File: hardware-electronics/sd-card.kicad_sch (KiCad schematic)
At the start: 40 parts, among them J5 Micro_SD_Card_Det_Hirose_DM3AT, U6 24AA04T-I_OT, U9 USB2244-AEZG-06, Y3 ECS-240-10-47-CKM-TR

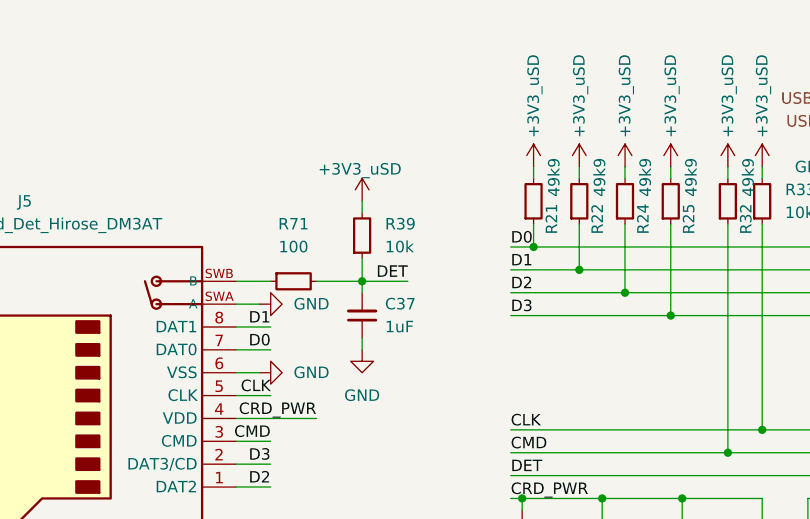
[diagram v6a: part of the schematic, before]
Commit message: [#16] uSD decreased cap reload time to aprox 10ms on DET pins
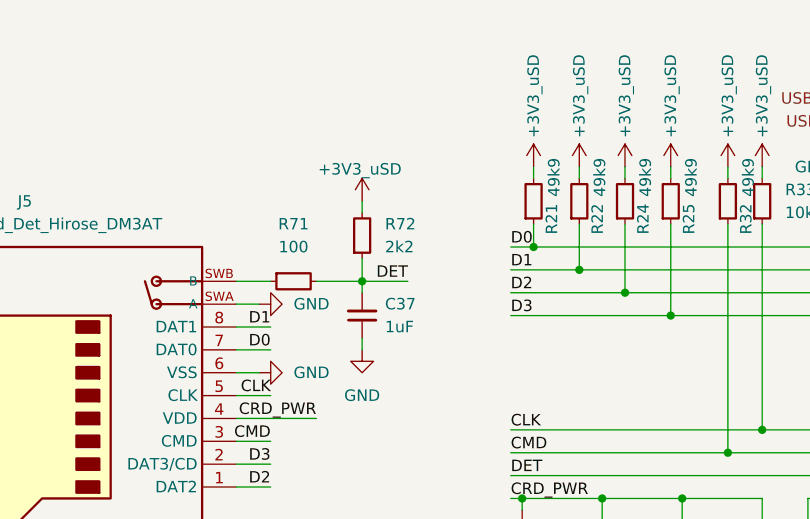
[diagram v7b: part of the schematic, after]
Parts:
- removed R39: R_10k_0402, M2SmartHomeFootprints:R_0402, symbol M2SmartHomeSymbols:R_10k_0402
- added R72: R_2k2_0402, M2SmartHomeFootprints:R_0402, symbol M2SmartHomeSymbols:R_2k2_0402
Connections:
- net +3V3_uSD: now also R72.2
- net DET: now also R72.1
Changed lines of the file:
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@@
-	)
-	(symbol
-		(lib_id "M2SmartHomeSymbols:R_10k_0402")
-		(at 78.74 72.39 90)
-		(unit 1)
-		(exclude_from_sim no)
-		(in_bom yes)
-		(on_board yes)
-		(dnp no)
-		(fields_autoplaced yes)
-		(property "Reference" "R39"
-			(at 81.28 68.58 90)
-			(effects
-				(font
-					(size 1.27 1.27)
-					(thickness 0.15)
-				)
-				(justify right)
-			)
-		)
-		(property "Value" "R_10k_0402"
-			(at 91.44 52.07 0)
-			(effects
-				(font
-					(size 1.27 1.27)
-					(thickness 0.15)
-				)
-				(justify left bottom)
-				(hide yes)
-			)
-		)
-		(property "Footprint" "M2SmartHomeFootprints:R_0402"
-			(at 93.98 52.07 0)
-			(effects
-				(font
-					(size 1.27 1.27)
-					(thickness 0.15)
-				)
-				(justify left bottom)
-				(hide yes)
-			)
-		)
-		(property "Datasheet" "https://www.vishay.com/docs/20035/crcw0402.pdf"
-			(at 96.52 52.07 0)
-			(effects
-				(font
-					(size 1.27 1.27)
-					(thickness 0.15)
-				)
-				(justify left bottom)
-				(hide yes)
-			)
-		)
-		(property "Description" "SMD Thick Film Resistor, 10 kΩ, ±1%, 1/16 W, 0402 [1005 Metric], CRCW Series"
-			(at 78.74 72.39 0)
-			(effects
-				(font
-					(size 1.27 1.27)
-				)
-				(hide yes)
-			)
-		)
-		(property "MPN" "CRCW040210K0FKED"
-			(at 99.06 52.07 0)
-			(effects
-				(font
-					(size 1.27 1.27)
-					(thickness 0.15)
-				)
-				(justify left bottom)
-				(hide yes)
-			)
-		)
-		(property "Manufacturer" "Vishay"
-			(at 101.6 52.07 0)
-			(effects
-				(font
-					(size 1.27 1.27)
-					(thickness 0.15)
-				)
-				(justify left bottom)
-				(hide yes)
-			)
-		)
-		(property "License" "Apache-2.0"
-			(at 104.14 52.07 0)
-			(effects
-				(font
-					(size 1.27 1.27)
-					(thickness 0.15)
-				)
-				(justify left bottom)
-				(hide yes)
-			)
-		)
-		(property "Author" "Your Name"
-			(at 106.68 52.07 0)
-			(effects
-				(font
-					(size 1.27 1.27)
-					(thickness 0.15)
-				)
-				(justify left bottom)
-				(hide yes)
-			)
-		)
-		(property "Val" "10k"
-			(at 81.28 71.12 90)
-			(effects
-				(font
-					(size 1.27 1.27)
-					(thickness 0.15)
-				)
-				(justify right)
-			)
-		)
-		(property "Tolerance" "1%"
-			(at 88.9 52.07 0)
-			(effects
-				(font
-					(size 1.27 1.27)
-				)
-				(justify left bottom)
-				(hide yes)
-			)
-		)
-		(property "Power" "1/16 W"
-			(at 92.44 52.07 0)
-			(effects
-				(font
-					(size 1.27 1.27)
-				)
-				(justify left bottom)
-				(hide yes)
-			)
-		)
-		(pin "1"
-		)
-		(pin "2"
-		)
-		(instances
-			(project "M2SmartHome"
-				(path "/da663dec-9e91-4003-a791-431d460ad63c/2a53ffe2-5715-44b3-b464-b3185e5be86d"
-					(reference "R39")
-					(unit 1)
-				)
-			)
-		)
 	)
 	(symbol
@@
 					(unit 1)
 				)
+			)
+		)
+	)
+	(symbol
+		(lib_id "M2SmartHomeSymbols:R_2k2_0402")
+		(at 78.74 72.39 90)
+		(unit 1)
+		(exclude_from_sim no)
+		(in_bom yes)
+		(on_board yes)
+		(dnp no)
+		(fields_autoplaced yes)
+		(property "Reference" "R72"
+			(at 81.28 68.58 90)
+			(effects
+				(font
+					(size 1.27 1.27)
+					(thickness 0.15)
+				)
+				(justify right)
+			)
+		)
+		(property "Value" "R_2k2_0402"
+			(at 91.44 52.07 0)
+			(effects
+				(font
+					(size 1.27 1.27)
+					(thickness 0.15)
+				)
+				(justify left bottom)
+				(hide yes)
+			)
+		)
+		(property "Footprint" "M2SmartHomeFootprints:R_0402"
+			(at 93.98 52.07 0)
+			(effects
+				(font
+					(size 1.27 1.27)
+					(thickness 0.15)
+				)
+				(justify left bottom)
+				(hide yes)
+			)
+		)
+		(property "Datasheet" "https://www.vishay.com/docs/20035/crcw0402.pdf"
+			(at 96.52 52.07 0)
+			(effects
+				(font
+					(size 1.27 1.27)
+					(thickness 0.15)
+				)
+				(justify left bottom)
+				(hide yes)
+			)
+		)
+		(property "Description" "SMD Thick Film Resistor, 2.2 kΩ, ±1%, 1/16 W, 0402 [1005 Metric], CRCW Series"
+			(at 78.74 72.39 0)
+			(effects
+				(font
+					(size 1.27 1.27)
+				)
+				(hide yes)
+			)
+		)
+		(property "MPN" "CRCW04022K20FKED"
+			(at 99.06 52.07 0)
+			(effects
+				(font
+					(size 1.27 1.27)
+					(thickness 0.15)
+				)
+				(justify left bottom)
+				(hide yes)
+			)
+		)
+		(property "Manufacturer" "Vishay"
+			(at 101.6 52.07 0)
+			(effects
+				(font
+					(size 1.27 1.27)
+					(thickness 0.15)
+				)
+				(justify left bottom)
+				(hide yes)
+			)
+		)
+		(property "License" "Apache-2.0"
+			(at 104.14 52.07 0)
+			(effects
+				(font
+					(size 1.27 1.27)
+					(thickness 0.15)
+				)
+				(justify left bottom)
+				(hide yes)
+			)
+		)
+		(property "Val" "2k2"
+			(at 81.28 71.12 90)
+			(effects
+				(font
+					(size 1.27 1.27)
+					(thickness 0.15)
+				)
+				(justify right)
+			)
+		)
+		(property "Tolerance" "1%"
+			(at 88.9 52.07 0)
+			(effects
+				(font
+					(size 1.27 1.27)
+				)
+				(justify left bottom)
+				(hide yes)
+			)
+		)
+		(property "Power" "1/16 W"
+			(at 92.44 52.07 0)
+			(effects
+				(font
+					(size 1.27 1.27)
+				)
+				(justify left bottom)
+				(hide yes)
+			)
+		)
+		(pin "1"
+		)
+		(pin "2"
+		)
+		(instances
+			(project "M2SmartHome"
+				(path "/da663dec-9e91-4003-a791-431d460ad63c/2a53ffe2-5715-44b3-b464-b3185e5be86d"
+					(reference "R72")
+					(unit 1)
+				)
